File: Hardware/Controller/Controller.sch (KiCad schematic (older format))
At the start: 60 parts, among them J1 8P8C, J2 LCD Header, J3 USB_B_Micro, J4 S88, J5 Screw_Terminal_01x05, SW1 Rotary_Encoder_Switch, SW2 SW_F0, SW3 SW_F1, SW4 SW_F2, SW5 SW_F3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

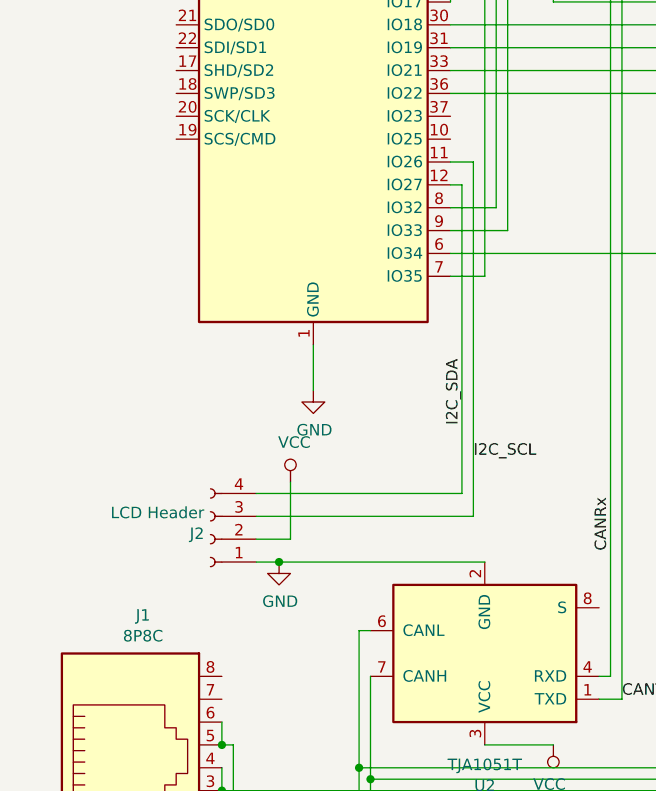
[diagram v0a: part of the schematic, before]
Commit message: Fixed part footprints
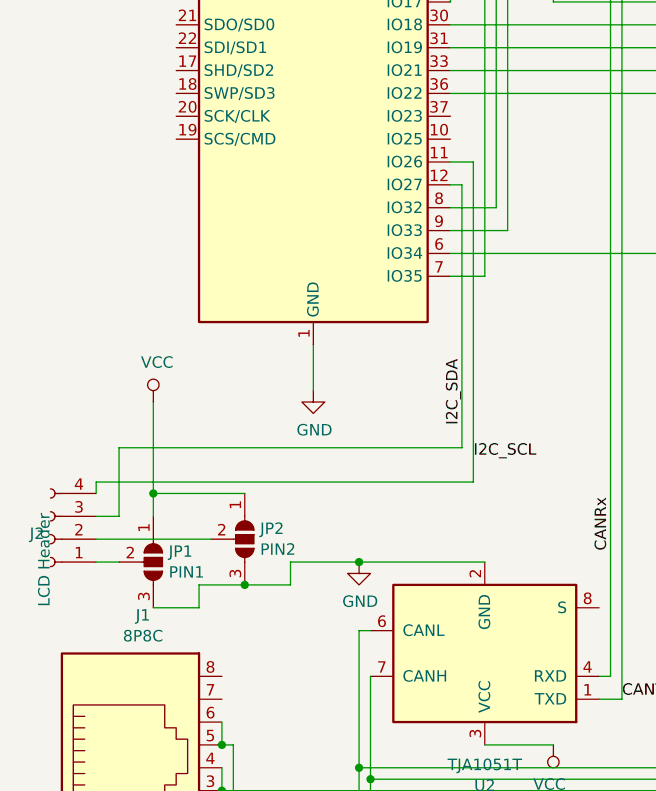
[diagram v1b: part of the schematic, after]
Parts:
- added JP1: PIN1, Jumper:SolderJumper-3_P1.3mm_Open_Pad1.0x1.5mm_NumberLabels, symbol Jumper:SolderJumper_3_Open
- added JP2: PIN2, Jumper:SolderJumper-3_P1.3mm_Open_Pad1.0x1.5mm_NumberLabels, symbol Jumper:SolderJumper_3_Open
- J4: footprint Connector_Molex:Molex_Micro-Latch_53254-0670_1x06_P2.00mm_Horizontal -> Connector_PinHeader_2.54mm:PinHeader_1x06_P2.54mm_Horizontal
- J5: footprint TerminalBlock_RND:TerminalBlock_RND_205-00015_1x05_P5.00mm_Horizontal -> TerminalBlock_4Ucon:TerminalBlock_4Ucon_1x05_P3.50mm_Vertical
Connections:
- net GND: now also JP1.3 (B), JP2.3 (B); no longer J2.1 (Pin_1)
- net I2C_SCL: now also J2.4 (Pin_4); no longer J2.3 (Pin_3)
- net I2C_SDA: now also J2.3 (Pin_3); no longer J2.4 (Pin_4)
- net VCC: now also JP1.1 (A), JP2.1 (A); no longer J2.2 (Pin_2)
- new net: J2.1 (Pin_1), JP1.2 (C)
- new net: J2.2 (Pin_2), JP2.2 (C)
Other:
- moved on the sheet: J2
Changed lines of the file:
@@
 F 0 "J4" H 6379 1142 50  0000 L CNN
 F 1 "S88" H 6379 1051 50  0000 L CNN
-F 2 "Connector_Molex:Molex_Micro-Latch_53254-0670_1x06_P2.00mm_Horizontal" H 6300 1150 50  0001 C CNN
+F 2 "Connector_PinHeader_2.54mm:PinHeader_1x06_P2.54mm_Horizontal" H 6300 1150 50  0001 C CNN
 F 3 "~" H 6300 1150 50  0001 C CNN
 	1    6300 1150
@@
 L power:GND #PWR0116
 U 1 1 5C737C70
-P 1600 5050
-F 0 "#PWR0116" H 1600 4800 50  0001 C CNN
-F 1 "GND" H 1605 4877 50  0000 C CNN
-F 2 "" H 1600 5050 50  0001 C CNN
-F 3 "" H 1600 5050 50  0001 C CNN
-	1    1600 5050
+P 1950 5050
+F 0 "#PWR0116" H 1950 4800 50  0001 C CNN
+F 1 "GND" H 1955 4877 50  0000 C CNN
+F 2 "" H 1950 5050 50  0001 C CNN
+F 3 "" H 1950 5050 50  0001 C CNN
+	1    1950 5050
 	1    0    0    -1
 $EndComp
@@
 L power:VCC #PWR0117
 U 1 1 5C737D53
-P 1650 4700
-F 0 "#PWR0117" H 1650 4550 50  0001 C CNN
-F 1 "VCC" H 1667 4873 50  0000 C CNN
-F 2 "" H 1650 4700 50  0001 C CNN
-F 3 "" H 1650 4700 50  0001 C CNN
-	1    1650 4700
-	1    0    0    -1
-$EndComp
-Wire Wire Line
-	2400 3400 2400 4750
-Wire Wire Line
-	2400 4750 1500 4750
-Wire Wire Line
-	2450 3300 2450 4850
-Wire Wire Line
-	2450 4850 1500 4850
+P 1050 4350
+F 0 "#PWR0117" H 1050 4200 50  0001 C CNN
+F 1 "VCC" H 1067 4523 50  0000 C CNN
+F 2 "" H 1050 4350 50  0001 C CNN
+F 3 "" H 1050 4350 50  0001 C CNN
+	1    1050 4350
+	1    0    0    -1
+$EndComp
+Wire Wire Line
+	2400 3400 2400 4550
+Wire Wire Line
+	2450 3300 2450 4700
 $Comp
 L power:GND #PWR0118
@@
 F 0 "J5" H 6630 7342 50  0000 L CNN
 F 1 "Screw_Terminal_01x05" H 6630 7251 50  0000 L CNN
-F 2 "TerminalBlock_RND:TerminalBlock_RND_205-00015_1x05_P5.00mm_Horizontal" H 6550 7300 50  0001 C CNN
+F 2 "TerminalBlock_4Ucon:TerminalBlock_4Ucon_1x05_P3.50mm_Vertical" H 6550 7300 50  0001 C CNN
 F 3 "~" H 6550 7300 50  0001 C CNN
 	1    6550 7300
@@
 Wire Wire Line
 	4250 7300 6350 7300
-Wire Wire Line
-	1500 5050 1600 5050
 $Comp
 L Connector:Conn_01x04_Female J2
 U 1 1 5C694C1B
-P 1300 4950
-F 0 "J2" H 1327 4926 50  0000 L CNN
-F 1 "LCD Header" H 1327 4835 50  0000 L CNN
-F 2 "Connector_PinHeader_2.54mm:PinHeader_1x04_P2.54mm_Vertical" H 1300 4950 50  0001 C CNN
-F 3 "~" H 1300 4950 50  0001 C CNN
-	1    1300 4950
+P 600 4950
+F 0 "J2" H 627 4926 50  0000 L CNN
+F 1 "LCD Header" V 627 4835 50  0000 L CNN
+F 2 "Connector_PinHeader_2.54mm:PinHeader_1x04_P2.54mm_Vertical" H 600 4950 50  0001 C CNN
+F 3 "~" H 600 4950 50  0001 C CNN
+	1    600  4950
 	-1   0    0    1
 $EndComp
 Wire Wire Line
-	1500 4950 1650 4950
-Wire Wire Line
-	1650 4950 1650 4700
-Wire Wire Line
-	1600 5050 2500 5050
-Connection ~ 1600 5050
+	1950 5050 2500 5050
 Wire Wire Line
 	1400 6950 2150 6950
@@
 Wire Wire Line
 	2450 3300 2350 3300
+$Comp
+L Jumper:SolderJumper_3_Open JP1
+U 1 1 5C9758C6
+P 1050 5050
+F 0 "JP1" V 1004 5117 50  0000 L CNN
+F 1 "PIN1" V 1095 5117 50  0000 L CNN
+F 2 "Jumper:SolderJumper-3_P1.3mm_Open_Pad1.0x1.5mm_NumberLabels" H 1050 5050 50  0001 C CNN
+F 3 "~" H 1050 5050 50  0001 C CNN
+	1    1050 5050
+	0    1    1    0
+$EndComp
+$Comp
+L Jumper:SolderJumper_3_Open JP2
+U 1 1 5C98D090
+P 1450 4950
+F 0 "JP2" V 1404 5017 50  0000 L CNN
+F 1 "PIN2" V 1495 5017 50  0000 L CNN
+F 2 "Jumper:SolderJumper-3_P1.3mm_Open_Pad1.0x1.5mm_NumberLabels" H 1450 4950 50  0001 C CNN
+F 3 "~" H 1450 4950 50  0001 C CNN
+	1    1450 4950
+	0    1    1    0
+$EndComp
+Wire Wire Line
+	800  5050 900  5050
+Wire Wire Line
+	800  4950 1300 4950
+Wire Wire Line
+	1050 4850 1050 4750
+Wire Wire Line
+	1450 4750 1050 4750
+Connection ~ 1050 4750
+Wire Wire Line
+	1050 4750 1050 4350
+Wire Wire Line
+	1950 5050 1650 5050
+Wire Wire Line
+	1650 5050 1650 5150
+Wire Wire Line
+	1650 5150 1450 5150
+Wire Wire Line
+	1250 5150 1250 5250
+Wire Wire Line
+	1250 5250 1050 5250
+Connection ~ 1950 5050
+Connection ~ 1450 5150
+Wire Wire Line
+	1450 5150 1250 5150
+Wire Wire Line
+	900  4550 2400 4550
+Wire Wire Line
+	800  4700 2450 4700
+Wire Wire Line
+	900  4550 900  4850
+Wire Wire Line
+	900  4850 800  4850
+Wire Wire Line
+	800  4700 800  4750
 $EndSCHEMATC

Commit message: Fixes for Manufacturing
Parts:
- removed D3: D_Schottky, Diode_SMD:D_0603_1608Metric_Pad1.05x0.95mm_HandSolder, symbol Device:D_Schottky
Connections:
- net VinTerminal is gone; now on net VinCAN: J5.3 (Pin_3)
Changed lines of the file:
@@
-$EndComp
-$Comp
-L Device:D_Schottky D3
-U 1 1 5C8637C0
-P 4500 6700
-F 0 "D3" H 4500 6916 50  0000 C CNN
-F 1 "D_Schottky" H 4500 6825 50  0000 C CNN
-F 2 "Diode_SMD:D_0603_1608Metric_Pad1.05x0.95mm_HandSolder" H 4500 6700 50  0001 C CNN
-F 3 "~" H 4500 6700 50  0001 C CNN
-	1    4500 6700
-	-1   0    0    1
 $EndComp
 $Comp
@@
 Wire Wire Line
 	4650 6350 4650 6700
-Wire Wire Line
-	4350 6700 4250 6700
-Wire Wire Line
-	4250 6700 4250 7300
-Wire Wire Line
-	4250 7300 6350 7300
 $Comp
 L Connector:Conn_01x04_Female J2
@@
 	4000 6100 4000 6350
 Wire Wire Line
-	4000 6350 4350 6350
-Wire Wire Line
 	1350 5950 1350 6050
 Wire Wire Line
@@
 Wire Wire Line
 	4000 6050 4000 5950
-Wire Wire Line
-	4000 5950 4350 5950
 Connection ~ 1350 6050
 Wire Wire Line
@@
 Wire Wire Line
 	4650 6700 4850 6700
-Connection ~ 4650 6700
 Connection ~ 4850 6700
 Wire Wire Line
@@
 Text Label 4400 7300 0    50   ~ 0
 VinTerminal
-Text Label 4050 6350 0    50   ~ 0
+Text Label 4150 6350 0    50   ~ 0
 VinUsb
-Text Label 4050 5950 0    50   ~ 0
+Text Label 4150 5950 0    50   ~ 0
 VinCAN
 Text Label 1500 7150 0    50   ~ 0
@@
 Wire Wire Line
 	800  4700 800  4750
+Wire Wire Line
+	4050 7300 6350 7300
+Wire Wire Line
+	4000 5950 4050 5950
+Wire Wire Line
+	4000 6350 4350 6350
+Wire Wire Line
+	4050 7300 4050 5950
+Connection ~ 4050 5950
+Wire Wire Line
+	4050 5950 4350 5950
 $EndSCHEMATC

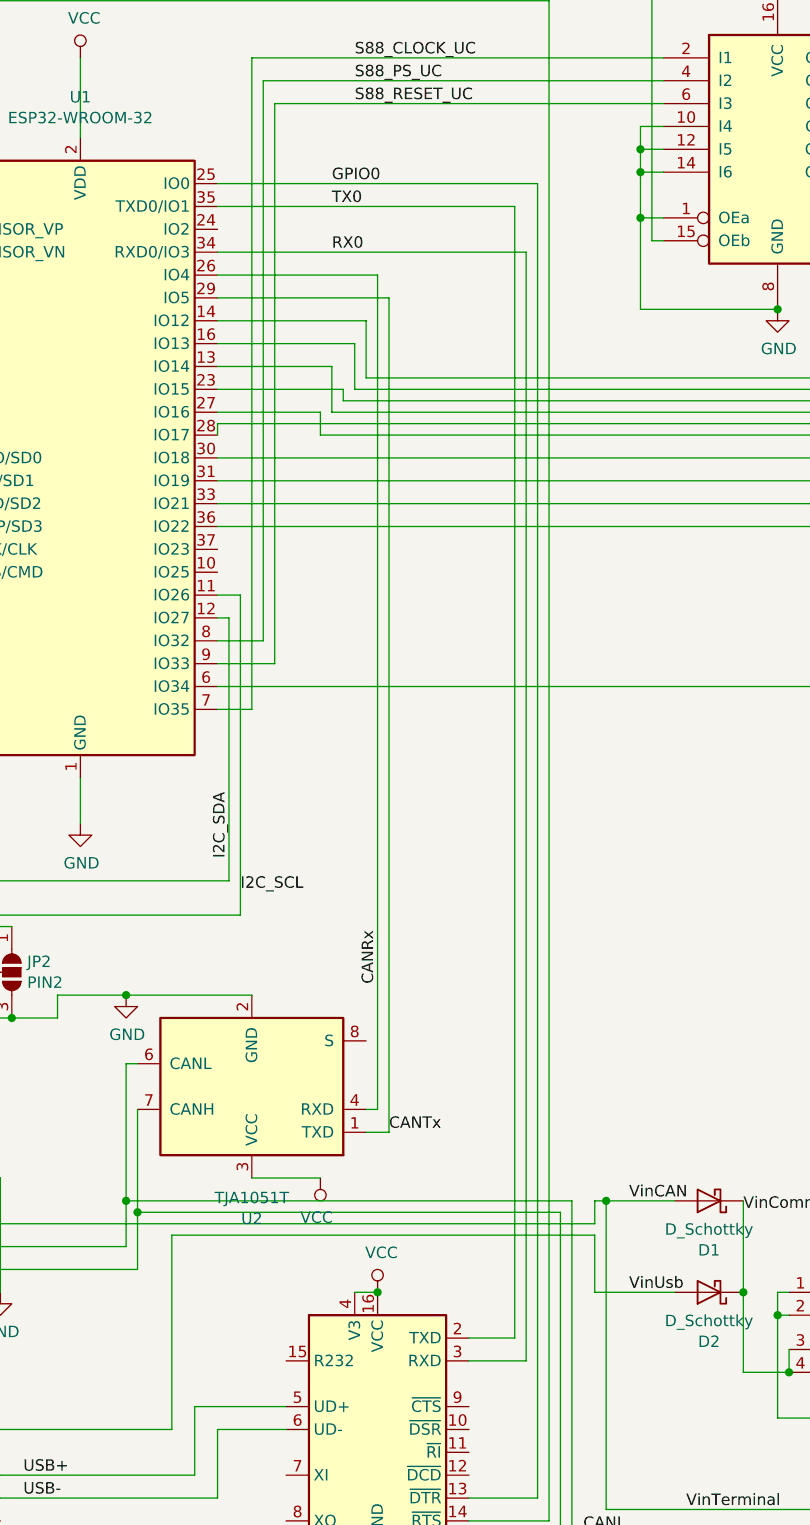
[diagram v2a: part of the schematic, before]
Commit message: Swap RX/TX
Fixes #1
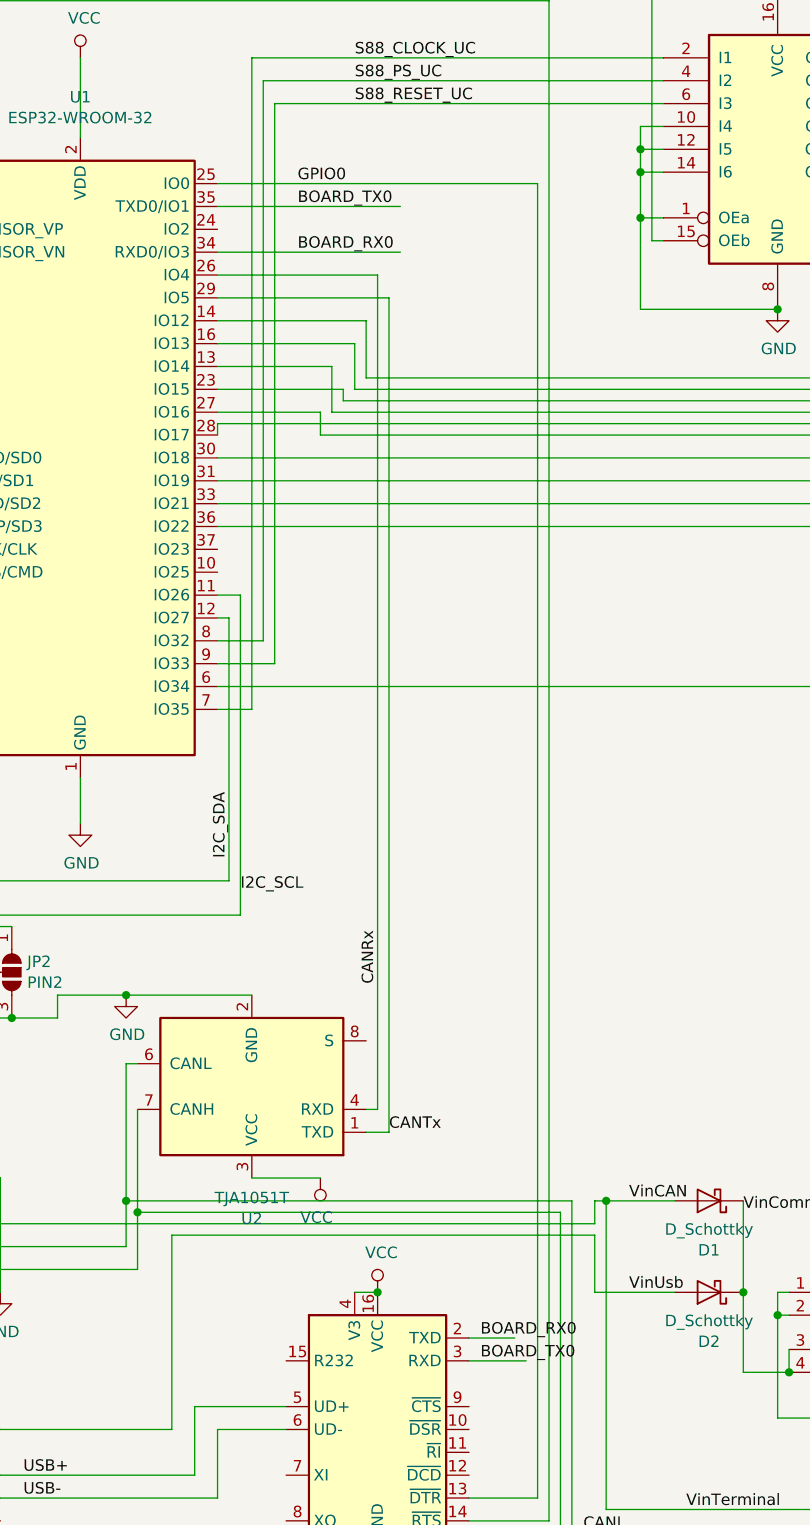
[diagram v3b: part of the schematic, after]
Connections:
- net RX0 renamed BOARD_RX0
- net BOARD_RX0: now also U4.2 (TXD); no longer U4.3 (RXD)
- net TX0 renamed BOARD_TX0
- net BOARD_TX0: now also U4.3 (RXD); no longer U4.2 (TXD)
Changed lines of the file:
@@
 	4250 650  4800 650
 Wire Wire Line
-	2350 1800 3700 1800
-Wire Wire Line
-	3700 1800 3700 6650
+	2350 1800 3150 1800
 Wire Wire Line
 	3700 6650 3450 6650
 Wire Wire Line
-	2350 1600 3650 1600
-Wire Wire Line
-	3650 1600 3650 6550
+	2350 1600 3150 1600
 Wire Wire Line
 	3650 6550 3450 6550
@@
 Text Label 9500 1050 0    50   ~ 0
 Encoder_Button
-Text Label 2850 1600 0    50   ~ 0
-TX0
-Text Label 2850 1800 0    50   ~ 0
-RX0
-Text Label 2850 1500 0    50   ~ 0
+Text Label 2700 1600 0    50   ~ 0
+BOARD_TX0
+Text Label 2700 1800 0    50   ~ 0
+BOARD_RX0
+Text Label 2700 1500 0    50   ~ 0
 GPIO0
 Text Label 2850 700  0    50   ~ 0
@@
 Wire Wire Line
 	4050 5950 4350 5950
+Text Label 3500 6650 0    50   ~ 0
+BOARD_TX0
+Text Label 3500 6550 0    50   ~ 0
+BOARD_RX0
 $EndSCHEMATC
